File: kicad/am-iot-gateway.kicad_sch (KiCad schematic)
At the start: 0 parts

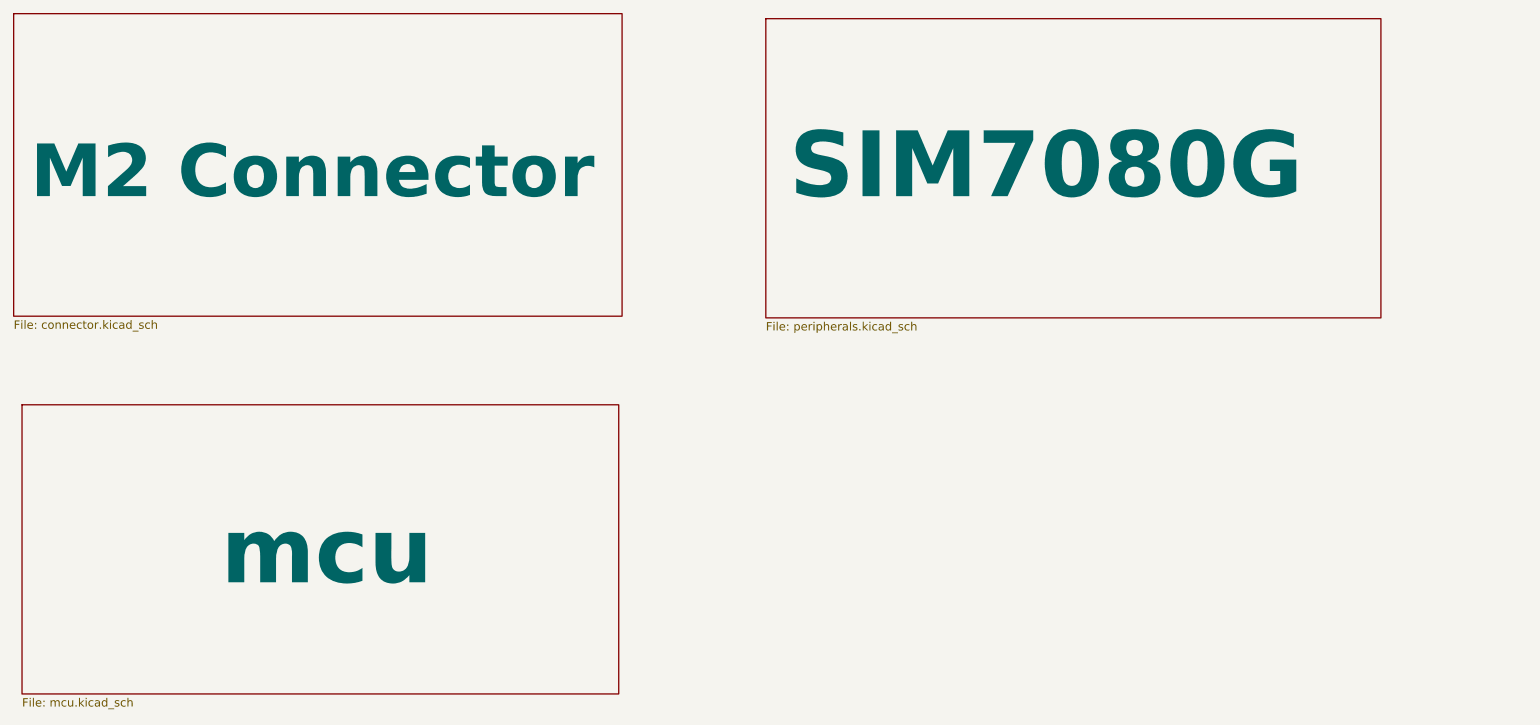
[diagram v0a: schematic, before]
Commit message: feat: minimal module with compute alone
Signed-off-by: Rodney Osodo <socials@rodneyosodo.com>
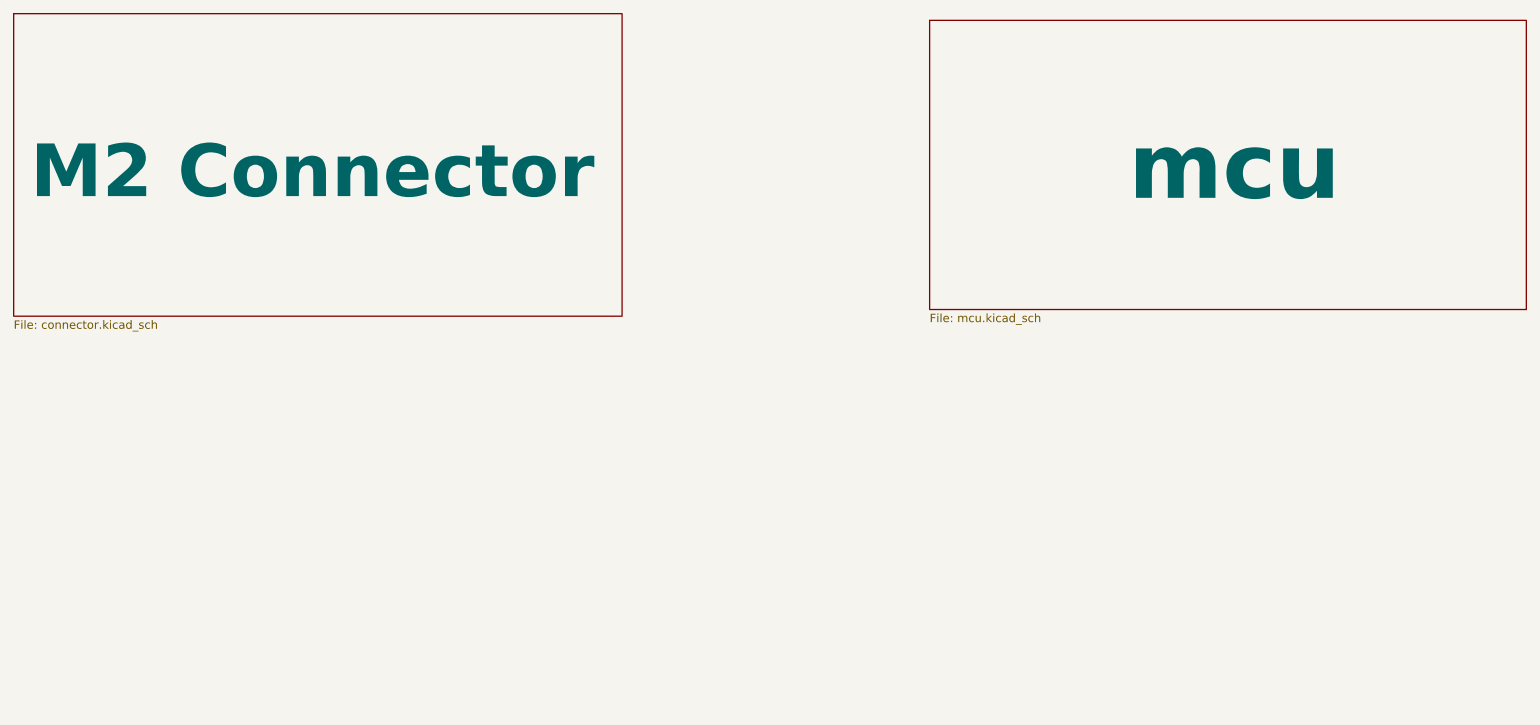
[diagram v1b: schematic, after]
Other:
- removed sheet SIM7080G
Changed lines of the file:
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@@
-	)
-	(sheet
-		(at 139.954 26.416)
-		(size 93.472 45.466)
-		(stroke
-			(width 0.1524)
-			(type solid)
-		)
-		(fill
-			(color 0 132 132 0.5000)
-		)
-		(property "Sheetname" "SIM7080G"
-			(at 143.51 54.61 0)
-			(effects
-				(font
-					(size 10 10)
-					(thickness 2)
-					(bold yes)
-				)
-				(justify left bottom)
-			)
-		)
-		(property "Sheetfile" "peripherals.kicad_sch"
-			(at 139.954 72.4666 0)
-			(effects
-				(font
-					(size 1.27 1.27)
-				)
-				(justify left top)
-			)
-		)
-		(instances
-			(project "am-iot-gateway"
-				(path "/9e4c0f80-14bc-451b-8b05-b2f0d1a90e15"
-					(page "4")
-				)
-			)
-		)
 	)
 	(sheet
@@
 	)
 	(sheet
-		(at 26.924 85.09)
+		(at 164.846 26.67)
 		(size 90.678 43.942)
 		(stroke
@@
 		)
 		(property "Sheetname" "mcu"
-			(at 57.15 113.284 0)
+			(at 195.072 54.864 0)
 			(effects
 				(font
@@
 		)
 		(property "Sheetfile" "mcu.kicad_sch"
-			(at 26.924 129.6166 0)
+			(at 164.846 71.1966 0)
 			(effects
 				(font
